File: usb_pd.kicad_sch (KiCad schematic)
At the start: 37 parts, among them J1 USB-C_GCT_USB4105-GF-A, J2 JST_SH_1x4_SM04B-SRSS-TB-LF-SN, Q1 SQS401EN-T1_BE3, U1 STUSB4500_QFN, U5 TPD4E02B04DQA, U6 TPD4E02B04DQA

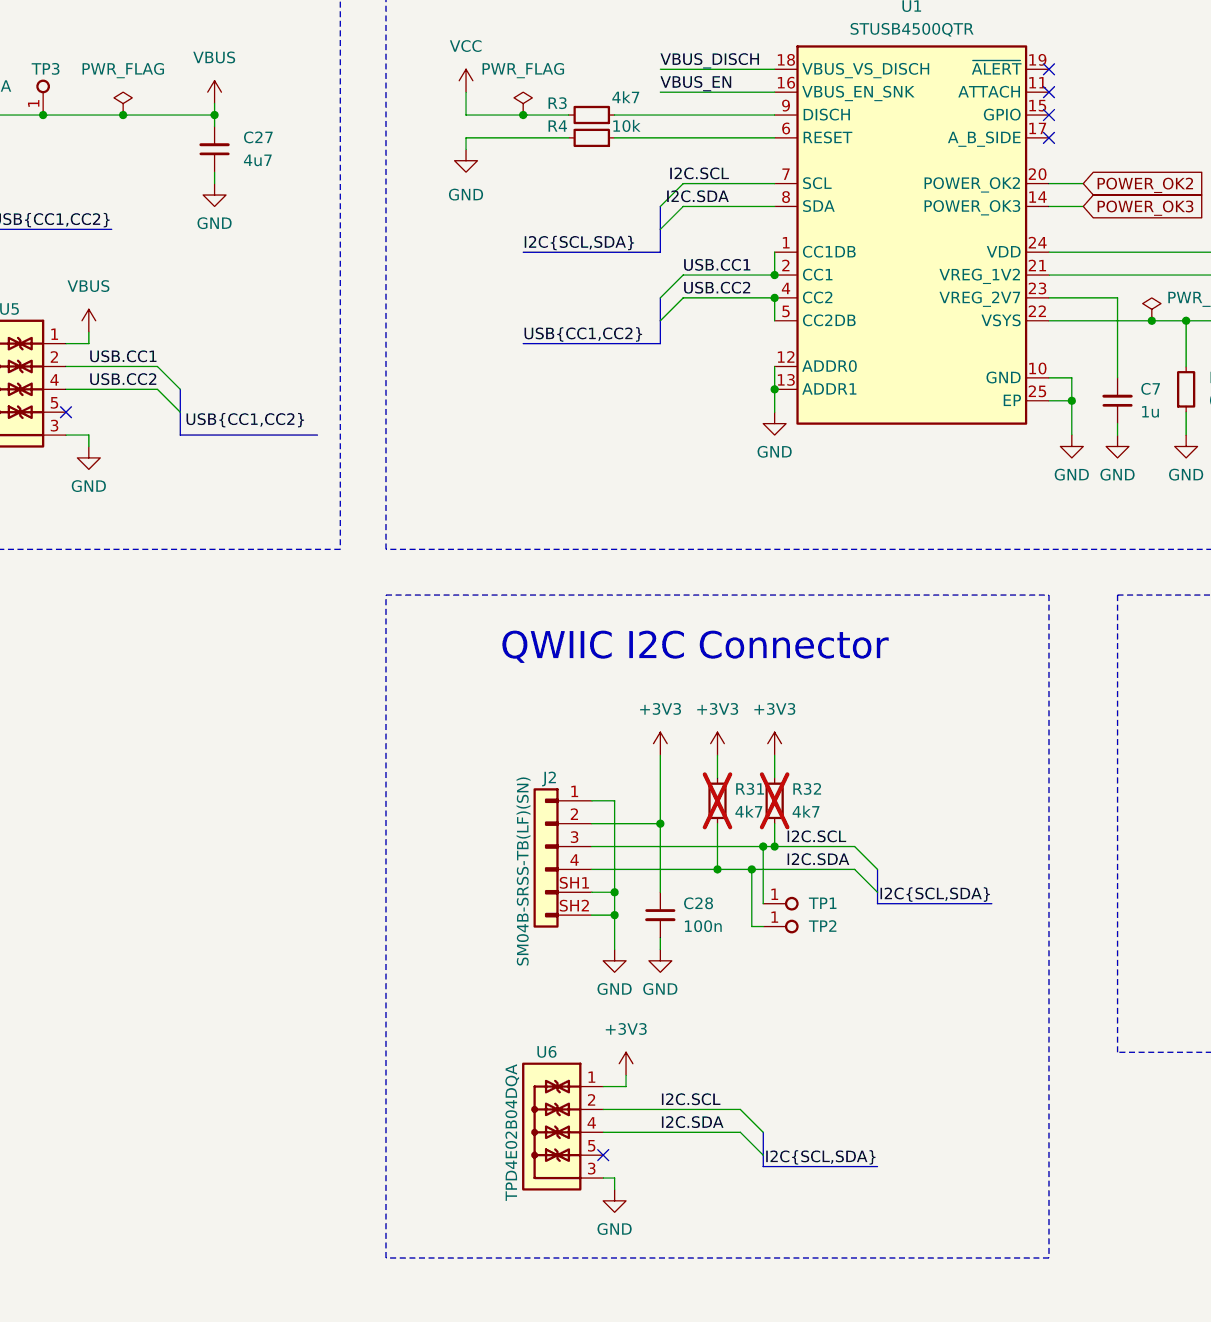
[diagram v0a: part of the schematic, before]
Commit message: [#57006] Add 0R resistor on 3v3 qwiic
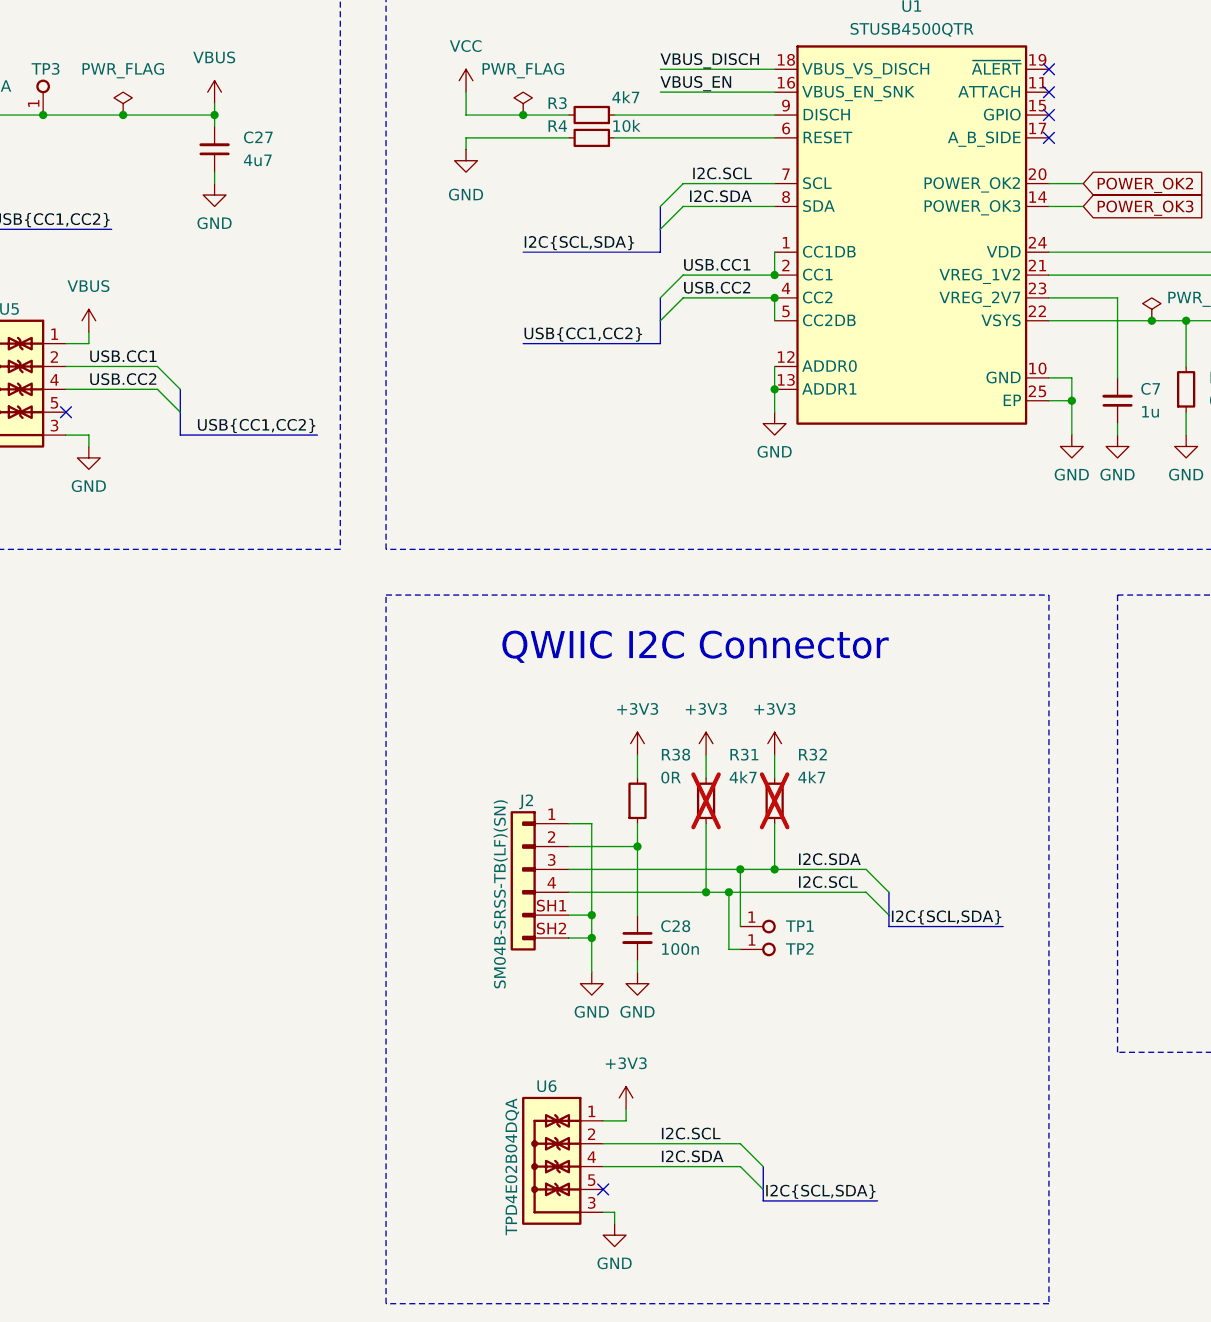
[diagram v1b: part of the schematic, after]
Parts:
- added R38: R_0R_0603, antmicro-footprints:R_0603_1608Metric, symbol antmicroResistors0603:R_0R_0603
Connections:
- net +3V3: now also R38.2; no longer C28.1, J2.2
- net I2C.SCL: now also J2.4, R31.1, TP2.1; no longer J2.3, R32.1, TP1.1
- net I2C.SDA: now also J2.3, R32.1, TP1.1; no longer J2.4, R31.1, TP2.1
- new net: C28.1, J2.2, R38.1
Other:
- moved on the sheet: C28, J2, R31, TP1, TP2, U6

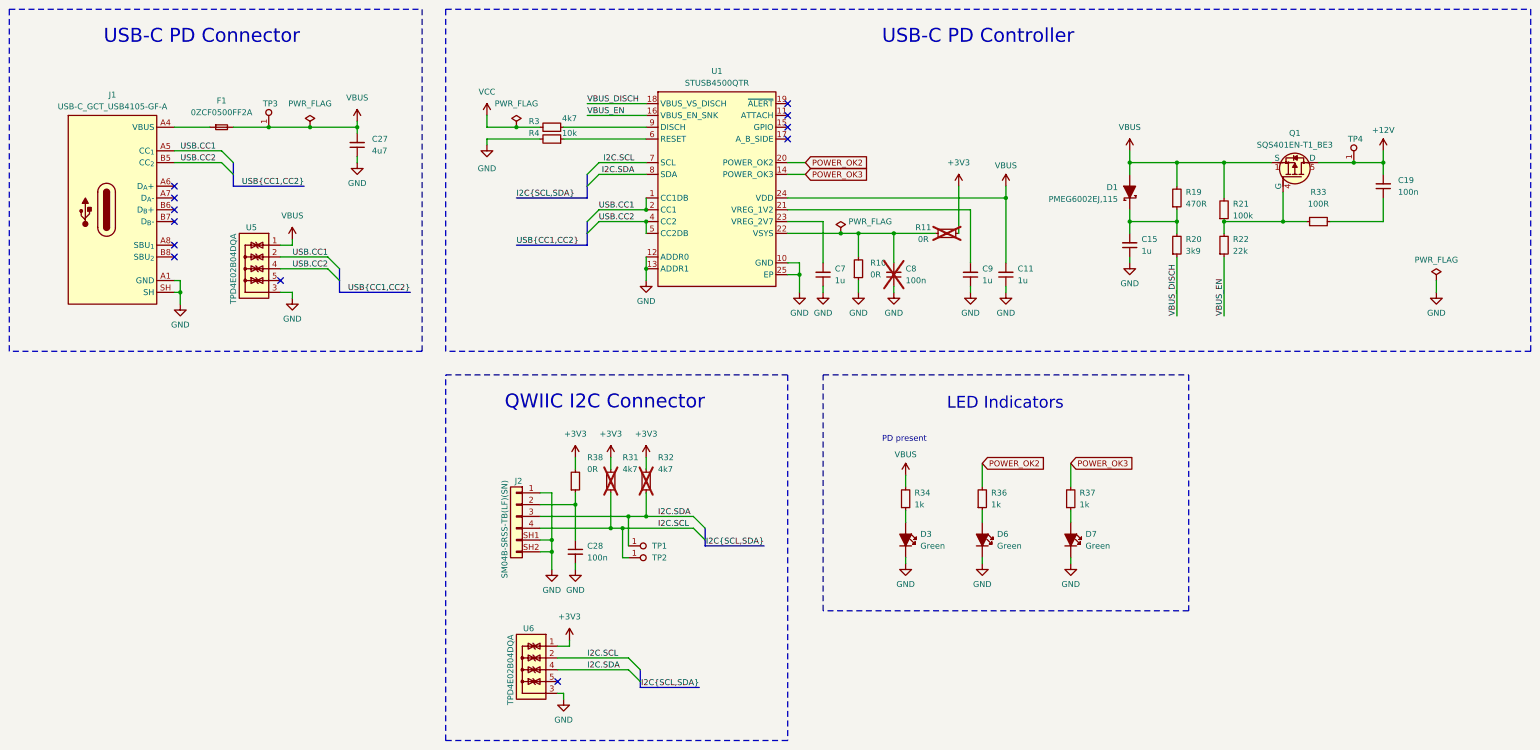
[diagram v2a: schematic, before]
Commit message: [#57006] Remove buses to improve readability
Change output power block's name
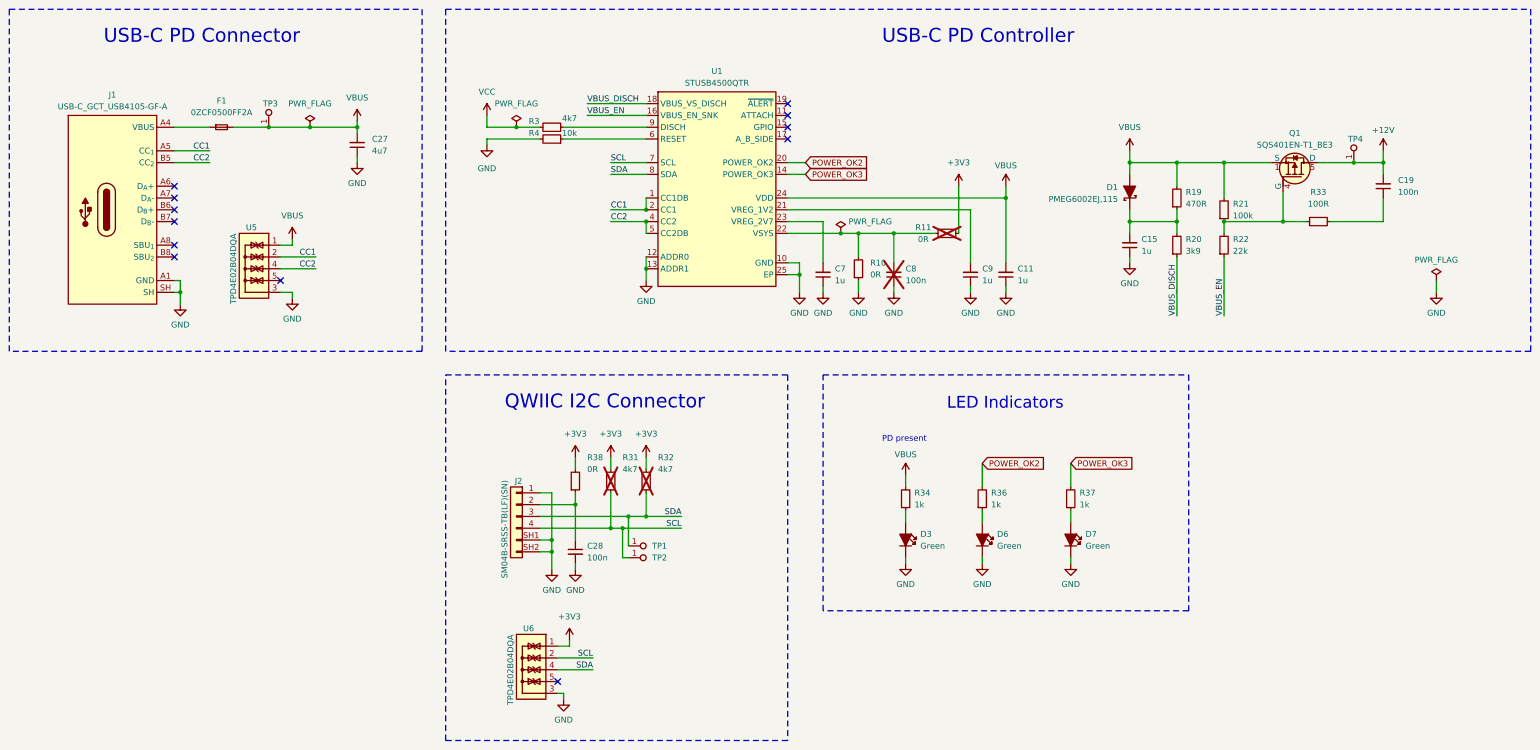
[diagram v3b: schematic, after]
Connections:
- net I2C.SCL renamed SCL
- net I2C.SDA renamed SDA
- net USB.CC1 renamed CC1
- net USB.CC2 renamed CC2

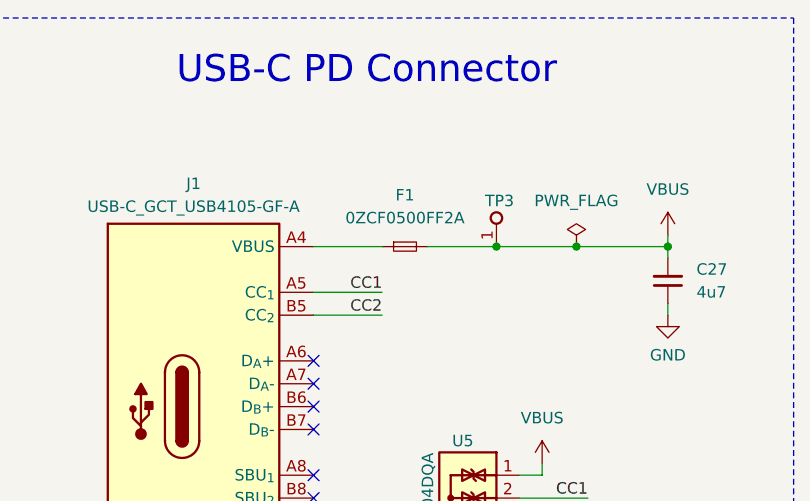
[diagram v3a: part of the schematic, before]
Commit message: [#57006] Remove fuse on VBUS input
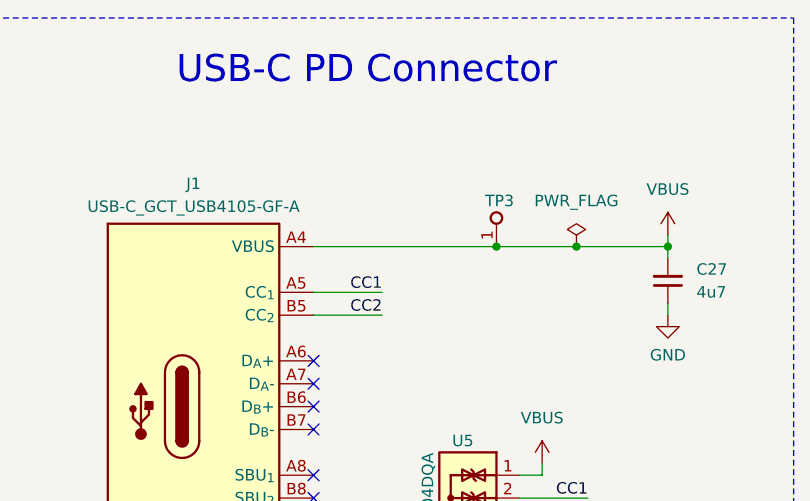
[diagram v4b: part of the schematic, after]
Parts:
- removed F1: F_5A_2920, antmicro-footprints:2920-fuse, symbol antmicroFuses:F_5A_2920
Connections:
- net VBUS: now also J1.A4 (VBUS), J1.A9 (VBUS), J1.B4 (VBUS), J1.B9 (VBUS)
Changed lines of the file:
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@@
     (stroke (width 0) (type default))
   )
-  (wire (pts (xy 66.04 53.34) (xy 73.66 53.34))
+  (wire (pts (xy 66.04 53.34) (xy 86.36 53.34))
     (stroke (width 0) (type default))
   )
@@
   )
   (wire (pts (xy 245.11 87.63) (xy 245.11 88.9))
-    (stroke (width 0) (type default))
-  )
-  (wire (pts (xy 78.74 53.34) (xy 86.36 53.34))
     (stroke (width 0) (type default))
   )
@@
         )
       )
-    )
-  )
-  (symbol (lib_id "antmicroFuses:F_5A_2920") (at 73.66 53.34 0) (unit 1)
-    (in_bom yes) (on_board yes) (dnp no) (fields_autoplaced)
-    (property "Reference" "F1" (at 76.2 47.625 0)
-      (effects (font (size 1.27 1.27) (thickness 0.15)))
-    )
-    (property "Value" "F_5A_2920" (at 93.98 60.96 0)
-      (effects (font (size 1.27 1.27) (thickness 0.15)) (justify left bottom) hide)
-    )
-    (property "Footprint" "antmicro-footprints:2920-fuse" (at 93.98 63.5 0)
-      (effects (font (size 1.27 1.27) (thickness 0.15)) (justify left bottom) hide)
-    )
-    (property "Datasheet" "https://www.mouser.com/datasheet/2/643/ds_CP_0zcf_series-1633784.pdf" (at 93.98 66.04 0)
-      (effects (font (size 1.27 1.27) (thickness 0.15)) (justify left bottom) hide)
-    )
-    (property "MPN" "0ZCF0500FF2A" (at 76.2 50.165 0)
-      (effects (font (size 1.27 1.27) (thickness 0.15)))
-    )
-    (property "Manufacturer" "Bel Fuse" (at 93.98 71.12 0)
-      (effects (font (size 1.27 1.27) (thickness 0.15)) (justify left bottom) hide)
-    )
-    (property "Author" "Antmicro" (at 93.98 73.66 0)
-      (effects (font (size 1.27 1.27) (thickness 0.15)) (justify left bottom) hide)
-    )
-    (property "License" "Apache-2.0" (at 93.98 76.2 0)
-      (effects (font (size 1.27 1.27) (thickness 0.15)) (justify left bottom) hide)
-    )
-    (pin "2")
-    (pin "1")
-    (instances
-      (project "USB-C-power-adapter"
-        (path "/8da33aa8-79ed-467a-95ed-bf58aa0d1db6/344e016f-20ec-4e27-ac78-d9a1e9a3533b"
-          (reference "F1") (unit 1)
-        )
-      )

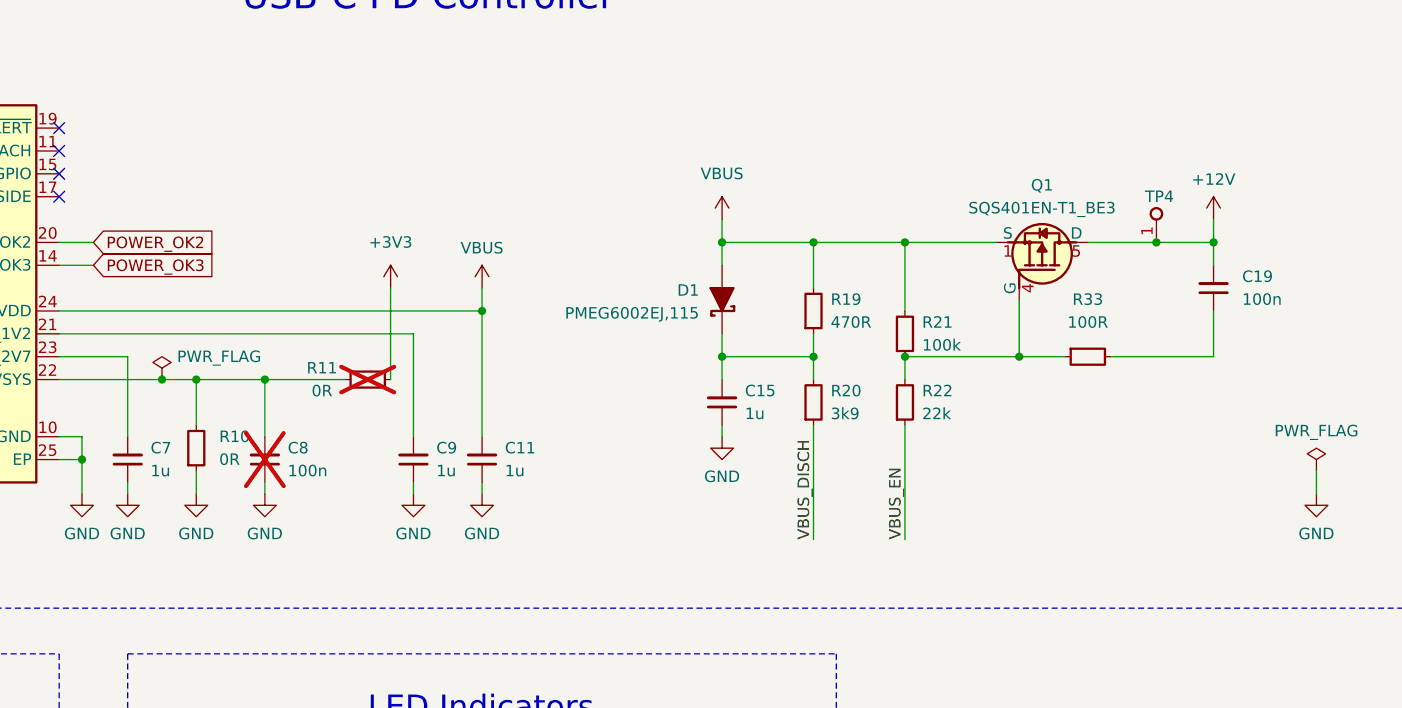
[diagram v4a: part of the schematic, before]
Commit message: [#57006] Fix wrong power label
Add +12V testpoint
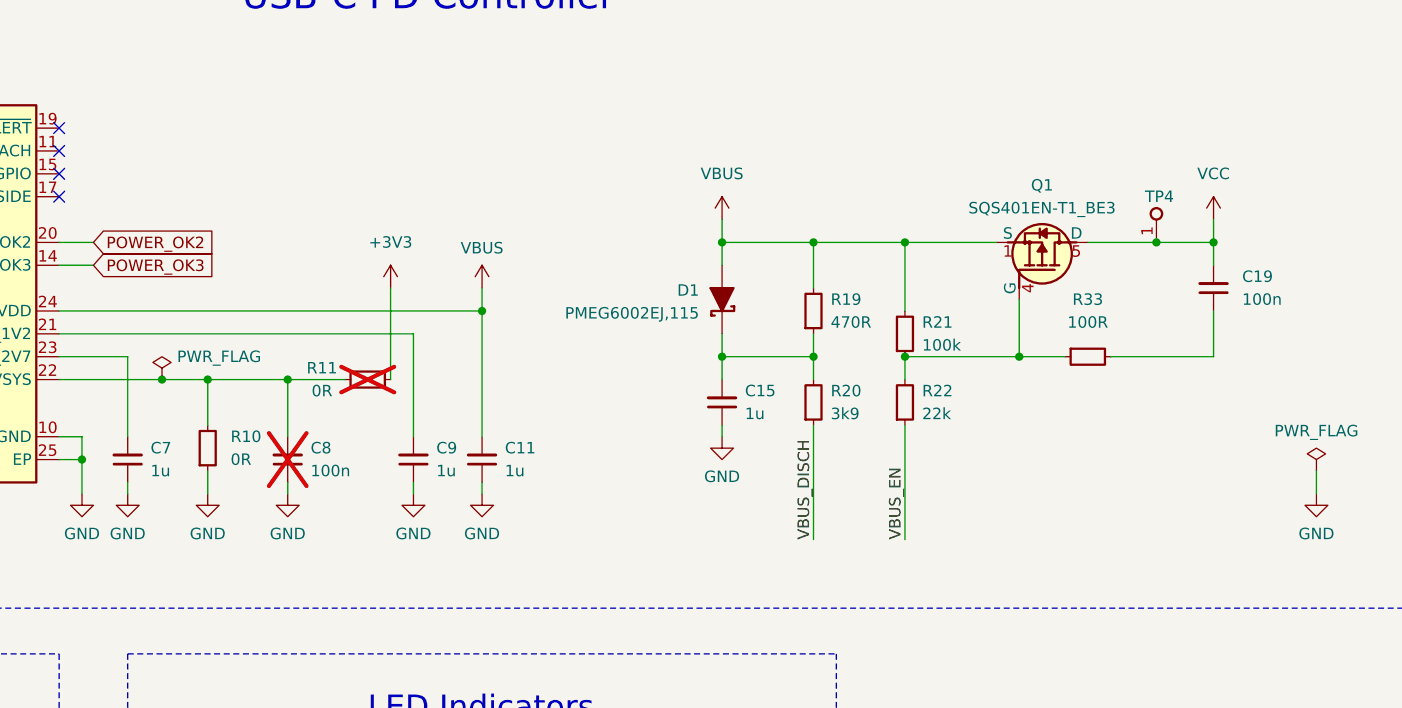
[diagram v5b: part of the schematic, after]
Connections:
- net +12V is gone; now on net VCC: C19.2, Q1.5 (D), TP4.1
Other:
- moved on the sheet: C8, R10
